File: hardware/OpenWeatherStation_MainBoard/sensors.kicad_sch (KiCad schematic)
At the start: 3 parts, among them U2 FXPS7115D4, U3 HTU21D

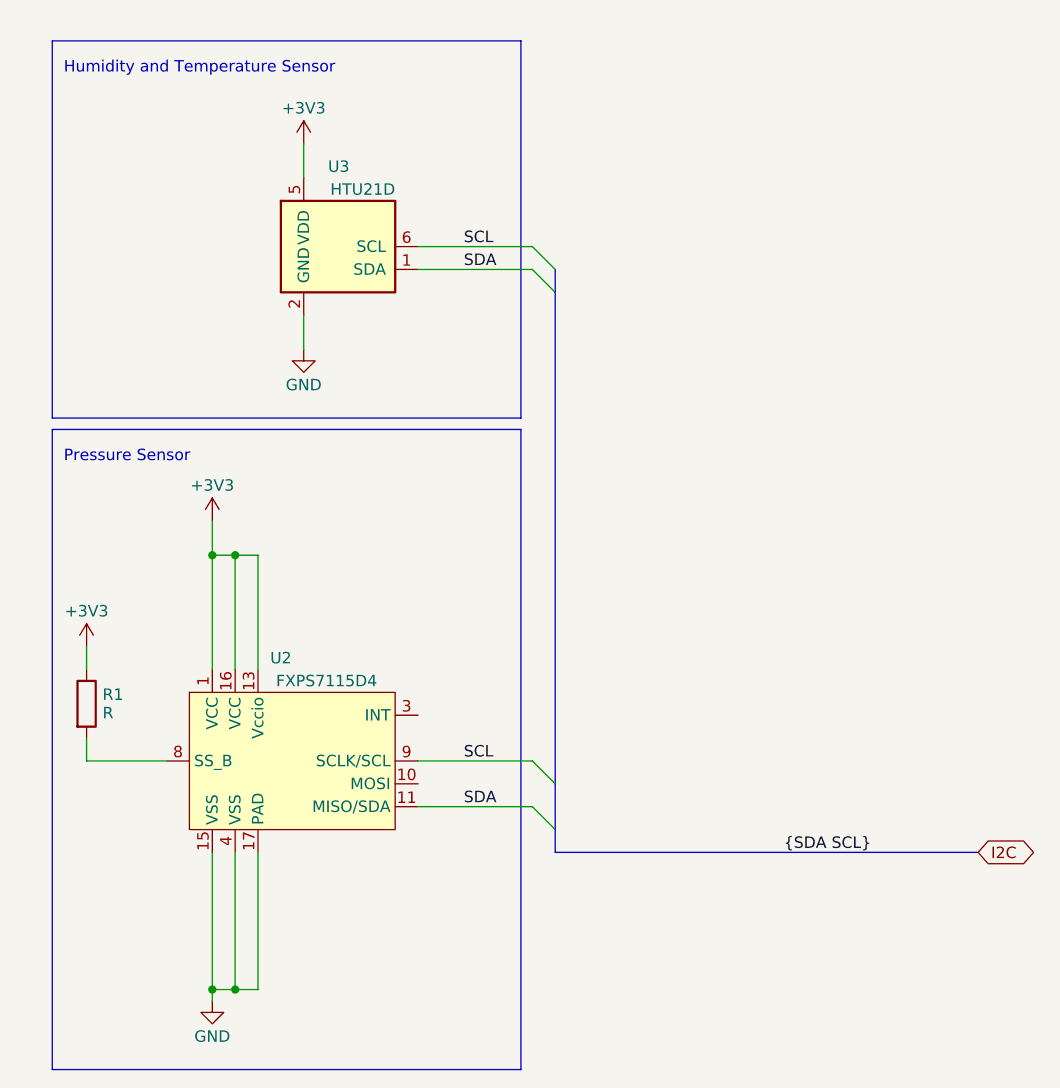
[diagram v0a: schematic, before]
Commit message: update board schematics (sensors, ethernet ...)
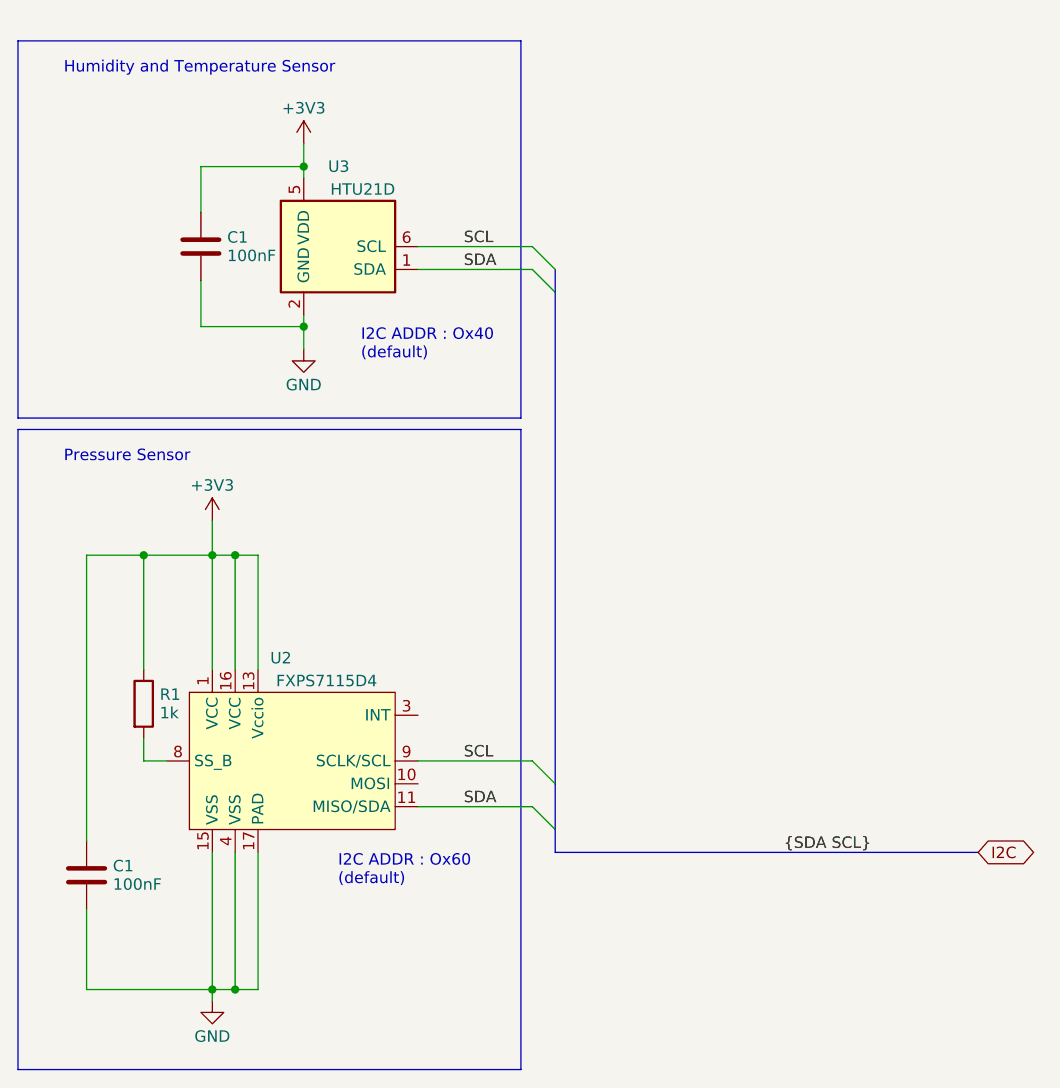
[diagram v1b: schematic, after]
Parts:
- added C1 (x2): 100nF, symbol Device:C
- R1: value R -> 1k
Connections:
- net +3V3: now also C1.1, C1.1
- net GND: now also C1.2, C1.2
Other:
- note added: "I2C ADDR : Ox40 (default)"
- note added: "I2C ADDR : Ox60 (default)"
- moved on the sheet: R1
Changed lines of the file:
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@@
 (kicad_sch (version 20230121) (generator eeschema)
   (paper "A4")
+  (junction (at 71.12 72.39) (diameter 0) (color 0 0 0 0)
+  )
   (junction (at 63.5 97.79) (diameter 0) (color 0 0 0 0)
   )
@@
   (junction (at 60.96 146.05) (diameter 0) (color 0 0 0 0)
   )
+  (junction (at 71.12 54.61) (diameter 0) (color 0 0 0 0)
+  )
   (junction (at 63.5 146.05) (diameter 0) (color 0 0 0 0)
   )
+  (junction (at 53.34 97.79) (diameter 0) (color 0 0 0 0)
+  )
   (bus_entry (at 96.52 120.65) (size 2.54 2.54)
     (stroke (width 0) (type default))
@@
     (stroke (width 0) (type default))
   )
+  (wire (pts (xy 46.99 137.16) (xy 46.99 146.05))
+    (stroke (width 0) (type default))
+  )
+  (wire (pts (xy 71.12 72.39) (xy 71.12 74.93))
+    (stroke (width 0) (type default))
+  )
   (bus (pts (xy 99.06 123.19) (xy 99.06 128.27))
     (stroke (width 0) (type default))
@@
     (stroke (width 0) (type default))
   )
-  (wire (pts (xy 46.99 107.95) (xy 46.99 110.49))
+  (wire (pts (xy 46.99 97.79) (xy 53.34 97.79))
+    (stroke (width 0) (type default))
+  )
+  (wire (pts (xy 53.34 97.79) (xy 53.34 110.49))
     (stroke (width 0) (type default))
   )
@@
     (stroke (width 0) (type default))
   )
-  (wire (pts (xy 71.12 52.07) (xy 71.12 55.88))
+  (wire (pts (xy 71.12 52.07) (xy 71.12 54.61))
+    (stroke (width 0) (type default))
+  )
+  (wire (pts (xy 59.69 67.31) (xy 59.69 72.39))
     (stroke (width 0) (type default))
   )
@@
     (stroke (width 0) (type default))
   )
+  (wire (pts (xy 59.69 72.39) (xy 71.12 72.39))
+    (stroke (width 0) (type default))
+  )
+  (wire (pts (xy 59.69 54.61) (xy 71.12 54.61))
+    (stroke (width 0) (type default))
+  )
   (bus (pts (xy 99.06 68.58) (xy 99.06 123.19))
     (stroke (width 0) (type default))
@@
     (stroke (width 0) (type default))
   )
-  (wire (pts (xy 71.12 71.12) (xy 71.12 74.93))
+  (wire (pts (xy 59.69 59.69) (xy 59.69 54.61))
+    (stroke (width 0) (type default))
+  )
+  (wire (pts (xy 71.12 71.12) (xy 71.12 72.39))
     (stroke (width 0) (type default))
   )
@@
     (stroke (width 0) (type default))
   )
+  (wire (pts (xy 46.99 129.54) (xy 46.99 97.79))
+    (stroke (width 0) (type default))
+  )
   (wire (pts (xy 83.82 125.73) (xy 96.52 125.73))
     (stroke (width 0) (type default))
   )
-  (wire (pts (xy 46.99 120.65) (xy 55.88 120.65))
+  (wire (pts (xy 53.34 120.65) (xy 55.88 120.65))
     (stroke (width 0) (type default))
   )
@@
     (stroke (width 0) (type default))
   )
-  (wire (pts (xy 46.99 120.65) (xy 46.99 118.11))
+  (wire (pts (xy 71.12 54.61) (xy 71.12 55.88))
+    (stroke (width 0) (type default))
+  )
+  (wire (pts (xy 53.34 120.65) (xy 53.34 118.11))
     (stroke (width 0) (type default))
   )
@@
     (stroke (width 0) (type default))
   )
+  (wire (pts (xy 53.34 97.79) (xy 60.96 97.79))
+    (stroke (width 0) (type default))
+  )
   (wire (pts (xy 60.96 130.81) (xy 60.96 146.05))
     (stroke (width 0) (type default))
@@
     (stroke (width 0) (type default))
   )
-  (rectangle (start 43.18 40.64) (end 95.25 82.55)
+  (wire (pts (xy 46.99 146.05) (xy 60.96 146.05))
+    (stroke (width 0) (type default))
+  )
+  (rectangle (start 39.37 40.64) (end 95.25 82.55)
     (stroke (width 0) (type default))
     (fill (type none))
   )
-  (rectangle (start 43.18 83.82) (end 95.25 154.94)
+  (rectangle (start 39.37 83.82) (end 95.25 154.94)
     (stroke (width 0) (type default))
     (fill (type none))
+  )
+  (text "I2C ADDR : Ox60\n(default)" (at 74.93 134.62 0)
+    (effects (font (size 1.27 1.27)) (justify left bottom))
+  )
+  (text "I2C ADDR : Ox40\n(default)" (at 77.47 76.2 0)
+    (effects (font (size 1.27 1.27)) (justify left bottom))
   )
   (text "Pressure Sensor" (at 44.45 87.63 0)
@@
         (path "/698c4dde-56a2-4dd1-89d2-180a09a5dfe9/e119c7c9-ed94-415e-ac5e-a04b52e23914"
           (reference "U3") (unit 1)
-        )
-      )
-    )
-  )
-  (symbol (lib_id "power:+3V3") (at 46.99 107.95 0) (unit 1)
-    (in_bom yes) (on_board yes) (dnp no) (fields_autoplaced)
-    (property "Reference" "#PWR08" (at 46.99 111.76 0)
-      (effects (font (size 1.27 1.27)) hide)
-    )
-    (property "Value" "+3V3" (at 46.99 104.005 0)
-      (effects (font (size 1.27 1.27)))
-    )
-    (property "Footprint" "" (at 46.99 107.95 0)
-      (effects (font (size 1.27 1.27)) hide)
-    )
-    (property "Datasheet" "" (at 46.99 107.95 0)
-      (effects (font (size 1.27 1.27)) hide)
-    )
-    (pin "1")
-    (instances
-      (project "OpenWeatherStation_MainBoard"
-        (path "/698c4dde-56a2-4dd1-89d2-180a09a5dfe9/e119c7c9-ed94-415e-ac5e-a04b52e23914"
-          (reference "#PWR08") (unit 1)
         )
       )
@@
     )
   )
-  (symbol (lib_id "Device:R") (at 46.99 114.3 0) (unit 1)
+  (symbol (lib_id "Device:R") (at 53.34 114.3 0) (unit 1)
     (in_bom yes) (on_board yes) (dnp no) (fields_autoplaced)
-    (property "Reference" "R1" (at 48.768 113.276 0)
-      (effects (font (size 1.27 1.27)) (justify left))
-    )
-    (property "Value" "R" (at 48.768 115.324 0)
-      (effects (font (size 1.27 1.27)) (justify left))
-    )
-    (property "Footprint" "" (at 45.212 114.3 90)
-      (effects (font (size 1.27 1.27)) hide)
-    )
-    (property "Datasheet" "~" (at 46.99 114.3 0)
+    (property "Reference" "R1" (at 55.118 113.276 0)
+      (effects (font (size 1.27 1.27)) (justify left))
+    )
+    (property "Value" "1k" (at 55.118 115.324 0)
+      (effects (font (size 1.27 1.27)) (justify left))
+    )
+    (property "Footprint" "" (at 51.562 114.3 90)
+      (effects (font (size 1.27 1.27)) hide)
+    )
+    (property "Datasheet" "~" (at 53.34 114.3 0)
       (effects (font (size 1.27 1.27)) hide)
     )
@@
         )
       )
+    )
+  )
+  (symbol (lib_id "Device:C") (at 59.69 63.5 0) (unit 1)
+    (in_bom yes) (on_board yes) (dnp no)
+    (property "Reference" "C1" (at 62.611 62.476 0)
+      (effects (font (size 1.27 1.27)) (justify left))
+    )
+    (property "Value" "100nF" (at 62.611 64.524 0)
+      (effects (font (size 1.27 1.27)) (justify left))
+    )
+    (property "Footprint" "" (at 60.6552 67.31 0)
+      (effects (font (size 1.27 1.27)) hide)
+    )
+    (property "Datasheet" "~" (at 59.69 63.5 0)
+      (effects (font (size 1.27 1.27)) hide)
+    )
+    (pin "1")
+    (pin "2")
+    (instances
+      (project "OpenWeatherStation_MainBoard"
+        (path "/698c4dde-56a2-4dd1-89d2-180a09a5dfe9/7c03bbc1-3816-4af6-9da6-b1bc735a9c60"
+          (reference "C1") (unit 1)
+        )
+        (path "/698c4dde-56a2-4dd1-89d2-180a09a5dfe9/e119c7c9-ed94-415e-ac5e-a04b52e23914"
+          (reference "C21") (unit 1)
+        )
+      )
+    )
+  )
+  (symbol (lib_id "Device:C") (at 46.99 133.35 0) (unit 1)
+    (in_bom yes) (on_board yes) (dnp no)
+    (property "Reference" "C1" (at 49.911 132.326 0)
+      (effects (font (size 1.27 1.27)) (justify left))
+    )
+    (property "Value" "100nF" (at 49.911 134.374 0)
+      (effects (font (size 1.27 1.27)) (justify left))
+    )
+    (property "Footprint" "" (at 47.9552 137.16 0)
+      (effects (font (size 1.27 1.27)) hide)
+    )
+    (property "Datasheet" "~" (at 46.99 133.35 0)
+      (effects (font (size 1.27 1.27)) hide)
+    )
+    (pin "1")
+    (pin "2")
+    (instances
+      (project "OpenWeatherStation_MainBoard"
+        (path "/698c4dde-56a2-4dd1-89d2-180a09a5dfe9/7c03bbc1-3816-4af6-9da6-b1bc735a9c60"
+          (reference "C1") (unit 1)
+        )
+        (path "/698c4dde-56a2-4dd1-89d2-180a09a5dfe9/e119c7c9-ed94-415e-ac5e-a04b52e23914"
+          (reference "C22") (unit 1)
+        )
+      )

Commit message: fix hierarchical bus
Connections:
- net SCL renamed I2C.SCL
- net SDA renamed I2C.SDA
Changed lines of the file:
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@@
   (junction (at 53.34 97.79) (diameter 0) (color 0 0 0 0)
   )
-  (bus_entry (at 96.52 120.65) (size 2.54 2.54)
+  (bus_entry (at 106.68 120.65) (size 2.54 2.54)
     (stroke (width 0) (type default))
   )
-  (bus_entry (at 96.52 63.5) (size 2.54 2.54)
+  (bus_entry (at 106.68 63.5) (size 2.54 2.54)
     (stroke (width 0) (type default))
   )
-  (bus_entry (at 96.52 125.73) (size 2.54 2.54)
+  (bus_entry (at 106.68 125.73) (size 2.54 2.54)
     (stroke (width 0) (type default))
   )
-  (bus_entry (at 96.52 66.04) (size 2.54 2.54)
+  (bus_entry (at 106.68 66.04) (size 2.54 2.54)
     (stroke (width 0) (type default))
   )
@@
     (stroke (width 0) (type default))
   )
-  (bus (pts (xy 99.06 66.04) (xy 99.06 68.58))
+  (bus (pts (xy 109.22 66.04) (xy 109.22 68.58))
     (stroke (width 0) (type default))
   )
@@
     (stroke (width 0) (type default))
   )
-  (bus (pts (xy 99.06 123.19) (xy 99.06 128.27))
+  (bus (pts (xy 109.22 123.19) (xy 109.22 128.27))
     (stroke (width 0) (type default))
   )
@@
     (stroke (width 0) (type default))
   )
-  (bus (pts (xy 99.06 130.81) (xy 146.05 130.81))
+  (bus (pts (xy 109.22 130.81) (xy 120.65 130.81))
     (stroke (width 0) (type default))
   )
@@
     (stroke (width 0) (type default))
   )
-  (bus (pts (xy 99.06 128.27) (xy 99.06 130.81))
+  (bus (pts (xy 109.22 128.27) (xy 109.22 130.81))
     (stroke (width 0) (type default))
   )
@@
     (stroke (width 0) (type default))
   )
-  (bus (pts (xy 99.06 68.58) (xy 99.06 123.19))
+  (bus (pts (xy 109.22 68.58) (xy 109.22 123.19))
     (stroke (width 0) (type default))
   )
@@
     (stroke (width 0) (type default))
   )
-  (wire (pts (xy 83.82 63.5) (xy 96.52 63.5))
+  (wire (pts (xy 83.82 63.5) (xy 106.68 63.5))
     (stroke (width 0) (type default))
   )
-  (wire (pts (xy 83.82 120.65) (xy 96.52 120.65))
+  (wire (pts (xy 83.82 120.65) (xy 106.68 120.65))
     (stroke (width 0) (type default))
   )
@@
     (stroke (width 0) (type default))
   )
-  (wire (pts (xy 83.82 125.73) (xy 96.52 125.73))
+  (wire (pts (xy 83.82 125.73) (xy 106.68 125.73))
     (stroke (width 0) (type default))
   )
@@
     (stroke (width 0) (type default))
   )
-  (wire (pts (xy 83.82 66.04) (xy 96.52 66.04))
+  (wire (pts (xy 83.82 66.04) (xy 106.68 66.04))
     (stroke (width 0) (type default))
   )
@@
     (effects (font (size 1.27 1.27)) (justify left bottom))
   )
-  (label "SDA" (at 88.9 66.04 0) (fields_autoplaced)
+  (label "I2C.SDA" (at 99.06 66.04 0) (fields_autoplaced)
     (effects (font (size 1.27 1.27)) (justify left bottom))
   )
-  (label "SCL" (at 88.9 120.65 0) (fields_autoplaced)
+  (label "I2C.SCL" (at 99.06 120.65 0) (fields_autoplaced)
     (effects (font (size 1.27 1.27)) (justify left bottom))
   )
-  (label "{SDA SCL}" (at 124.46 130.81 0) (fields_autoplaced)
+  (label "I2C.SCL" (at 99.06 63.5 0) (fields_autoplaced)
     (effects (font (size 1.27 1.27)) (justify left bottom))
   )
-  (label "SCL" (at 88.9 63.5 0) (fields_autoplaced)
+  (label "I2C.SDA" (at 99.06 125.73 0) (fields_autoplaced)
     (effects (font (size 1.27 1.27)) (justify left bottom))
   )
-  (label "SDA" (at 88.9 125.73 0) (fields_autoplaced)
-    (effects (font (size 1.27 1.27)) (justify left bottom))
-  )
-  (global_label "I2C" (shape bidirectional) (at 146.05 130.81 0) (fields_autoplaced)
+  (hierarchical_label "I2C{SDA SCL}" (shape bidirectional) (at 120.65 130.81 0) (fields_autoplaced)
     (effects (font (size 1.27 1.27)) (justify left))
-    (property "Intersheetrefs" "${INTERSHEET_REFS}" (at 152.3384 130.81 0)
-      (effects (font (size 1.27 1.27)) (justify left) hide)
-    )
   )
   (symbol (lib_id "power:+3V3") (at 71.12 52.07 0) (unit 1)

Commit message: schematic update
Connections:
- no-connect marks 0 -> 5
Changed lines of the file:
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@@
   (junction (at 53.34 97.79) (diameter 0) (color 0 0 0 0)
   )
+  (no_connect (at 73.66 110.49))
+  (no_connect (at 76.2 110.49))
+  (no_connect (at 71.12 110.49))
+  (no_connect (at 83.82 115.57))
+  (no_connect (at 83.82 123.19))
   (bus_entry (at 106.68 120.65) (size 2.54 2.54)
     (stroke (width 0) (type default))

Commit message: poe wip
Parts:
- renumbered C1 to C21, C1 to C22
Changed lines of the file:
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@@
   (symbol (lib_id "Device:C") (at 59.69 63.5 0) (unit 1)
     (in_bom yes) (on_board yes) (dnp no)
-    (property "Reference" "C1" (at 62.611 62.476 0)
+    (property "Reference" "C21" (at 62.611 62.476 0)
       (effects (font (size 1.27 1.27)) (justify left))
     )
@@
     (instances
       (project "OpenWeatherStation_MainBoard"
-        (path "/698c4dde-56a2-4dd1-89d2-180a09a5dfe9/7c03bbc1-3816-4af6-9da6-b1bc735a9c60"
-          (reference "C1") (unit 1)
-        )
         (path "/698c4dde-56a2-4dd1-89d2-180a09a5dfe9/e119c7c9-ed94-415e-ac5e-a04b52e23914"
           (reference "C21") (unit 1)
@@
   (symbol (lib_id "Device:C") (at 46.99 133.35 0) (unit 1)
     (in_bom yes) (on_board yes) (dnp no)
-    (property "Reference" "C1" (at 49.911 132.326 0)
+    (property "Reference" "C22" (at 49.911 132.326 0)
       (effects (font (size 1.27 1.27)) (justify left))
     )
@@
     (instances
       (project "OpenWeatherStation_MainBoard"
-        (path "/698c4dde-56a2-4dd1-89d2-180a09a5dfe9/7c03bbc1-3816-4af6-9da6-b1bc735a9c60"
-          (reference "C1") (unit 1)
-        )
         (path "/698c4dde-56a2-4dd1-89d2-180a09a5dfe9/e119c7c9-ed94-415e-ac5e-a04b52e23914"
           (reference "C22") (unit 1)

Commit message: electrical design wip
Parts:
- C21, C22: footprint (none) -> Capacitor_SMD:C_0603_1608Metric
- R1: footprint (none) -> Resistor_SMD:R_0603_1608Metric
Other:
- company: (none) -> Vital Septfonds
- title: (none) -> Open Wheather Station
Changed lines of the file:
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@@
 (kicad_sch (version 20230121) (generator eeschema)
   (paper "A4")
+  (title_block
+    (title "Open Wheather Station")
+    (date "2024-01-02")
+    (rev "1.0")
+    (company "Vital Septfonds")
+  )
   (junction (at 71.12 72.39) (diameter 0) (color 0 0 0 0)
   )
@@
       (effects (font (size 1.27 1.27)) (justify left))
     )
-    (property "Footprint" "" (at 51.562 114.3 90)
+    (property "Footprint" "Resistor_SMD:R_0603_1608Metric" (at 51.562 114.3 90)
       (effects (font (size 1.27 1.27)) hide)
     )
@@
       (effects (font (size 1.27 1.27)) (justify left))
     )
-    (property "Footprint" "" (at 60.6552 67.31 0)
+    (property "Footprint" "Capacitor_SMD:C_0603_1608Metric" (at 60.6552 67.31 0)
       (effects (font (size 1.27 1.27)) hide)
     )
@@
       (effects (font (size 1.27 1.27)) (justify left))
     )
-    (property "Footprint" "" (at 47.9552 137.16 0)
-      (effects (font (size 1.27 1.27)) hide)
-    )
+    (property "Footprint" "Capacitor_SMD:C_0603_1608Metric" (at 47.9552 137.16 0)
+      (effects (font (size 1.27 1.27)) hide)
+    )
